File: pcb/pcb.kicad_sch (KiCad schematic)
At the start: 23 parts, among them J1 Conn_02x04_Odd_Even, J10 Conn_02x04_Odd_Even, J11 Conn_02x04_Odd_Even, J12 Conn_02x04_Odd_Even, J13 Conn_02x04_Odd_Even, J14 Conn_02x04_Odd_Even, J15 Conn_02x04_Odd_Even, J16 Conn_02x04_Odd_Even, J17 Conn_02x04_Odd_Even, J18 Conn_02x04_Odd_Even, J19 Conn_02x04_Odd_Even, J2 Conn_02x04_Odd_Even, J20 Conn_02x04_Odd_Even, J21 Conn_01x04_Pin, J3 Conn_02x04_Odd_Even, J4 Conn_02x04_Odd_Even, J5 Conn_02x04_Odd_Even, J6 Conn_02x04_Odd_Even, J7 Conn_02x04_Odd_Even, J8 Conn_02x04_Odd_Even, J9 Conn_02x04_Odd_Even

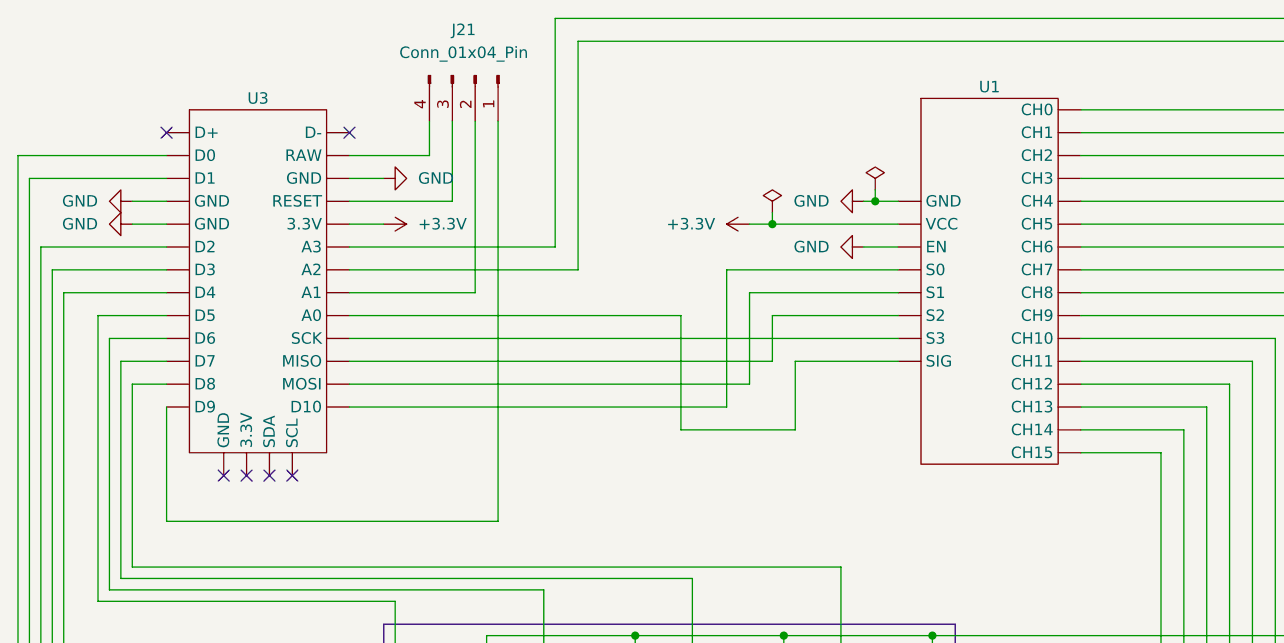
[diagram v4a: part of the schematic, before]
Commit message: header in documentation fixed, pcb schematic done
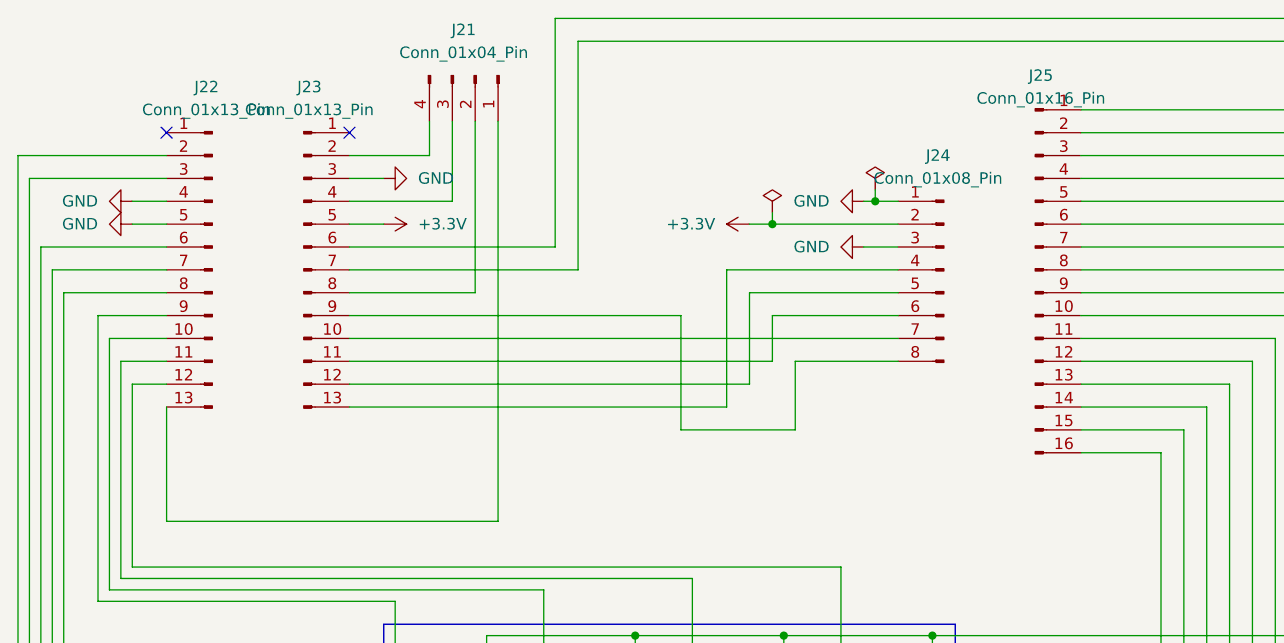
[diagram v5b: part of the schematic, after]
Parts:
- removed U1: ~, symbol analog_multiplexer:multiplexer
- removed U3: ~, symbol KB2040:KB2040
- added J22, J23: Conn_01x13_Pin, Connector_PinSocket_2.54mm:PinSocket_1x13_P2.54mm_Vertical, symbol Connector:Conn_01x13_Pin
- added J24: Conn_01x08_Pin, Connector_PinSocket_2.54mm:PinSocket_1x08_P2.54mm_Vertical, symbol Connector:Conn_01x08_Pin
- added J25: Conn_01x16_Pin, Connector_PinSocket_2.54mm:PinSocket_1x16_P2.54mm_Vertical, symbol Connector:Conn_01x16_Pin
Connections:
- net +3.3V: now also J23.5 (Pin_5), J24.2 (Pin_2)
- net GND: now also J22.4 (Pin_4), J22.5 (Pin_5), J23.3 (Pin_3), J24.1 (Pin_1), J24.3 (Pin_3)
- net at J14.3 (Pin_3): now also J25.10 (Pin_10)
- net at J10.4 (Pin_4), J14.4 (Pin_4), J18.4 (Pin_4)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: now also J22.10 (Pin_10)
- net at J13.6 (Pin_6), J14.6 (Pin_6), J15.6 (Pin_6)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: now also J22.7 (Pin_7)
- net at J1.7 (Pin_7), J10.7 (Pin_7), J11.7 (Pin_7)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: now also J23.6 (Pin_6)
- net at J1.8 (Pin_8), J10.8 (Pin_8), J11.8 (Pin_8)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: now also J23.7 (Pin_7)
- net at J21.1 (Pin_1): now also J22.13 (Pin_13)
- net at J21.2 (Pin_2): now also J23.8 (Pin_8)
- net at J21.3 (Pin_3): now also J23.4 (Pin_4)
- net at J21.4 (Pin_4): now also J23.2 (Pin_2)
- net at J6.3 (Pin_3): now also J25.2 (Pin_2)
- net at J5.6 (Pin_6), J6.6 (Pin_6), J7.6 (Pin_6)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: now also J22.3 (Pin_3)
- net at J10.3 (Pin_3): now also J25.6 (Pin_6)
- net at J10.6 (Pin_6), J11.6 (Pin_6), J12.6 (Pin_6)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: now also J22.6 (Pin_6)
- net at J5.3 (Pin_3): now also J25.1 (Pin_1)
- net at J1.4 (Pin_4), J13.4 (Pin_4), J17.4 (Pin_4)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: now also J22.9 (Pin_9)
- net at J12.3 (Pin_3): now also J25.8 (Pin_8)
- net at J12.4 (Pin_4), J16.4 (Pin_4), J20.4 (Pin_4)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: now also J22.12 (Pin_12)
- net at J20.3 (Pin_3): now also J25.16 (Pin_16)
- net at J17.6 (Pin_6), J18.6 (Pin_6), J19.6 (Pin_6)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: now also J22.8 (Pin_8)
- net at J1.6 (Pin_6), J2.6 (Pin_6), J3.6 (Pin_6)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: now also J22.2 (Pin_2)
- net at J13.3 (Pin_3): now also J25.9 (Pin_9)
- net at J18.3 (Pin_3): now also J25.14 (Pin_14)
- net at J7.3 (Pin_3): now also J25.3 (Pin_3)
- net at J11.4 (Pin_4), J15.4 (Pin_4), J19.4 (Pin_4)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: now also J22.11 (Pin_11)
- net at J11.3 (Pin_3): now also J25.7 (Pin_7)
- net at J17.3 (Pin_3): now also J25.13 (Pin_13)
- net at J16.3 (Pin_3): now also J25.12 (Pin_12)
- net at J15.3 (Pin_3): now also J25.11 (Pin_11)
- net at J9.3 (Pin_3): now also J25.5 (Pin_5)
- net at J8.3 (Pin_3): now also J25.4 (Pin_4)
- net at J19.3 (Pin_3): now also J25.15 (Pin_15)
- new net: J23.13 (Pin_13), J24.4 (Pin_4)
- new net: J23.12 (Pin_12), J24.5 (Pin_5)
- new net: J23.11 (Pin_11), J24.6 (Pin_6)
- new net: J23.10 (Pin_10), J24.7 (Pin_7)
- new net: J23.9 (Pin_9), J24.8 (Pin_8)
- no-connect marks 30 -> 26
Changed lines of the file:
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@@
   (no_connect (at 92.71 137.16))
   (no_connect (at 125.73 243.84))
-  (no_connect (at 54.61 66.04))
-  (no_connect (at 49.53 66.04))
   (no_connect (at 125.73 101.6))
   (no_connect (at 92.71 172.72))
@@
   (no_connect (at 123.19 243.84))
   (no_connect (at 92.71 208.28))
-  (no_connect (at 52.07 66.04))
   (no_connect (at 43.18 27.94))
   (no_connect (at 76.2 101.6))
   (no_connect (at 73.66 243.84))
   (no_connect (at 109.22 101.6))
-  (no_connect (at 57.15 66.04))
   (no_connect (at 76.2 208.28))
   (no_connect (at 92.71 101.6))
@@
     )
   )
+  (symbol (lib_id "Connector:Conn_01x13_Pin") (at 48.26 43.18 0) (mirror y) (unit 1)
+    (in_bom yes) (on_board yes) (dnp no)
+    (property "Reference" "J22" (at 47.625 22.86 0)
+      (effects (font (size 1.27 1.27)))
+    )
+    (property "Value" "Conn_01x13_Pin" (at 47.625 25.4 0)
+      (effects (font (size 1.27 1.27)))
+    )
+    (property "Footprint" "Connector_PinSocket_2.54mm:PinSocket_1x13_P2.54mm_Vertical" (at 48.26 43.18 0)
+      (effects (font (size 1.27 1.27)) hide)
+    )
+    (property "Datasheet" "~" (at 48.26 43.18 0)
+      (effects (font (size 1.27 1.27)) hide)
+    )
+    (pin "9")
+    (pin "13")
+    (pin "5")
+    (pin "8")
+    (pin "6")
+    (pin "7")
+    (pin "1")
+    (pin "12")
+    (pin "4")
+    (pin "10")
+    (pin "11")
+    (pin "2")
+    (pin "3")
+    (instances
+      (project "pcb"
+        (path "/7cd41366-658c-4c64-bfa9-b0a6b780fad4"
+          (reference "J22") (unit 1)
+        )
+      )
+    )
+  )
+  (symbol (lib_id "Connector:Conn_01x08_Pin") (at 129.54 43.18 0) (mirror y) (unit 1)
+    (in_bom yes) (on_board yes) (dnp no)
+    (property "Reference" "J24" (at 128.905 30.48 0)
+      (effects (font (size 1.27 1.27)))
+    )
+    (property "Value" "Conn_01x08_Pin" (at 128.905 33.02 0)
+      (effects (font (size 1.27 1.27)))
+    )
+    (property "Footprint" "Connector_PinSocket_2.54mm:PinSocket_1x08_P2.54mm_Vertical" (at 129.54 43.18 0)
+      (effects (font (size 1.27 1.27)) hide)
+    )
+    (property "Datasheet" "~" (at 129.54 43.18 0)
+      (effects (font (size 1.27 1.27)) hide)
+    )
+    (pin "1")
+    (pin "8")
+    (pin "6")
+    (pin "3")
+    (pin "7")
+    (pin "5")
+    (pin "4")
+    (pin "2")
+    (instances
+      (project "pcb"
+        (path "/7cd41366-658c-4c64-bfa9-b0a6b780fad4"
+          (reference "J24") (unit 1)
+        )
+      )
+    )
+  )
   (symbol (lib_id "power:GND") (at 104.14 243.84 0) (unit 1)
     (in_bom yes) (on_board yes) (dnp no) (fields_autoplaced)
@@
     )
   )
-  (symbol (lib_id "KB2040:KB2040") (at 53.34 41.91 0) (unit 1)
-    (in_bom yes) (on_board yes) (dnp no) (fields_autoplaced)
-    (property "Reference" "U3" (at 53.34 24.13 0)
-      (effects (font (size 1.27 1.27)))
-    )
-    (property "Value" "~" (at 57.15 36.83 0)
-      (effects (font (size 1.27 1.27)))
-    )
-    (property "Footprint" "" (at 57.15 36.83 0)
-      (effects (font (size 1.27 1.27)) hide)
-    )
-    (property "Datasheet" "" (at 57.15 36.83 0)
-      (effects (font (size 1.27 1.27)) hide)
-    )
-    (pin "")
-    (pin "")
-    (pin "")
-    (pin "")
-    (pin "")
-    (pin "")
-    (pin "")
-    (pin "")
-    (pin "")
-    (pin "")
-    (pin "")
-    (pin "")
-    (pin "")
-    (pin "")
-    (pin "")
-    (pin "")
-    (pin "")
-    (pin "")
-    (pin "")
-    (pin "")
-    (pin "")
-    (pin "")
-    (pin "")
-    (pin "")
-    (pin "")
-    (pin "")
-    (pin "")
-    (pin "")
-    (pin "")
-    (pin "")
-    (instances
-      (project "pcb"
-        (path "/7cd41366-658c-4c64-bfa9-b0a6b780fad4"
-          (reference "U3") (unit 1)
-        )
-      )
-    )
-  )
   (symbol (lib_id "Connector_Generic:Conn_02x04_Odd_Even") (at 123.19 132.08 90) (unit 1)
     (in_bom yes) (on_board yes) (dnp no)
@@
     )
   )
-  (symbol (lib_name "multiplexer_1") (lib_id "analog_multiplexer:multiplexer") (at 134.62 45.72 0) (unit 1)
-    (in_bom yes) (on_board yes) (dnp no) (fields_autoplaced)
-    (property "Reference" "U1" (at 134.62 22.86 0)
-      (effects (font (size 1.27 1.27)))
-    )
-    (property "Value" "~" (at 133.35 46.99 0)
-      (effects (font (size 1.27 1.27)))
-    )
-    (property "Footprint" "" (at 133.35 46.99 0)
-      (effects (font (size 1.27 1.27)) hide)
-    )
-    (property "Datasheet" "" (at 133.35 46.99 0)
-      (effects (font (size 1.27 1.27)) hide)
-    )
-    (pin "")
-    (pin "")
-    (pin "")
-    (pin "")
-    (pin "")
-    (pin "")
-    (pin "")
-    (pin "")
-    (pin "")
-    (pin "")
-    (pin "")
-    (pin "")
-    (pin "")
-    (pin "")
-    (pin "")
-    (pin "")
-    (pin "")
-    (pin "")
-    (pin "")
-    (pin "")
-    (pin "")
-    (pin "")
-    (pin "")
-    (pin "")
-    (instances
-      (project "pcb"
-        (path "/7cd41366-658c-4c64-bfa9-b0a6b780fad4"
-          (reference "U1") (unit 1)
-        )
-      )
-    )
-  )
   (symbol (lib_id "power:GND") (at 120.65 172.72 0) (unit 1)
     (in_bom yes) (on_board yes) (dnp no) (fields_autoplaced)
@@
     )
   )
+  (symbol (lib_id "Connector:Conn_01x13_Pin") (at 58.42 43.18 0) (unit 1)
+    (in_bom yes) (on_board yes) (dnp no)
+    (property "Reference" "J23" (at 59.055 22.86 0)
+      (effects (font (size 1.27 1.27)))
+    )
+    (property "Value" "Conn_01x13_Pin" (at 59.055 25.4 0)
+      (effects (font (size 1.27 1.27)))
+    )
+    (property "Footprint" "Connector_PinSocket_2.54mm:PinSocket_1x13_P2.54mm_Vertical" (at 58.42 43.18 0)
+      (effects (font (size 1.27 1.27)) hide)
+    )
+    (property "Datasheet" "~" (at 58.42 43.18 0)
+      (effects (font (size 1.27 1.27)) hide)
+    )
+    (pin "9")
+    (pin "13")
+    (pin "5")
+    (pin "8")
+    (pin "6")
+    (pin "7")
+    (pin "1")
+    (pin "12")
+    (pin "4")
+    (pin "10")
+    (pin "11")
+    (pin "2")
+    (pin "3")
+    (instances
+      (project "pcb"
+        (path "/7cd41366-658c-4c64-bfa9-b0a6b780fad4"
+          (reference "J23") (unit 1)
+        )
+      )
+    )
+  )
   (symbol (lib_id "power:+3.3V") (at 120.65 160.02 0) (unit 1)
     (in_bom yes) (on_board yes) (dnp no) (fields_autoplaced)
@@
         )
       )
+    )
+  )
+  (symbol (lib_id "Connector:Conn_01x16_Pin") (at 139.7 43.18 0) (unit 1)
+    (in_bom yes) (on_board yes) (dnp no) (fields_autoplaced)
+    (property "Reference" "J25" (at 140.335 21.59 0)
+      (effects (font (size 1.27 1.27)))
+    )
+    (property "Value" "Conn_01x16_Pin" (at 140.335 24.13 0)
+      (effects (font (size 1.27 1.27)))
+    )
+    (property "Footprint" "Connector_PinSocket_2.54mm:PinSocket_1x16_P2.54mm_Vertical" (at 139.7 43.18 0)
+      (effects (font (size 1.27 1.27)) hide)
+    )
+    (property "Datasheet" "~" (at 139.7 43.18 0)
+      (effects (font (size 1.27 1.27)) hide)
+    )
+    (pin "1")
+    (pin "5")
+    (pin "13")
+    (pin "4")
+    (pin "3")
+    (pin "7")
+    (pin "2")
+    (pin "6")
+    (pin "8")
+    (pin "15")
+    (pin "9")
+    (pin "11")
+    (pin "10")
+    (pin "12")
+    (pin "16")
+    (pin "14")
+    (instances
+      (project "pcb"
+        (path "/7cd41366-658c-4c64-bfa9-b0a6b780fad4"
+          (reference "J25") (unit 1)
+        )
+      )

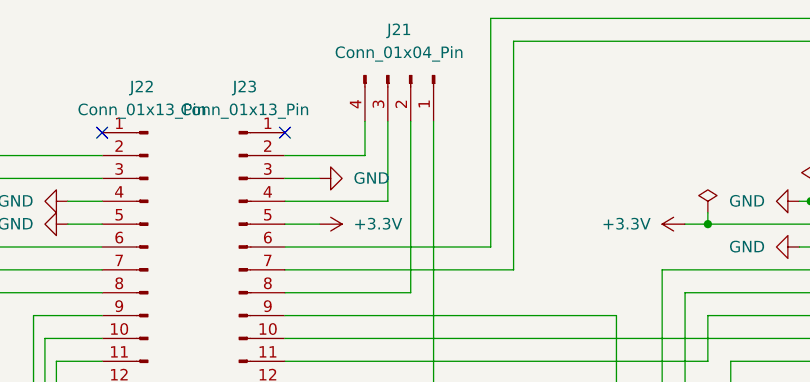
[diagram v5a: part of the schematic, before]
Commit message: pcb component placement
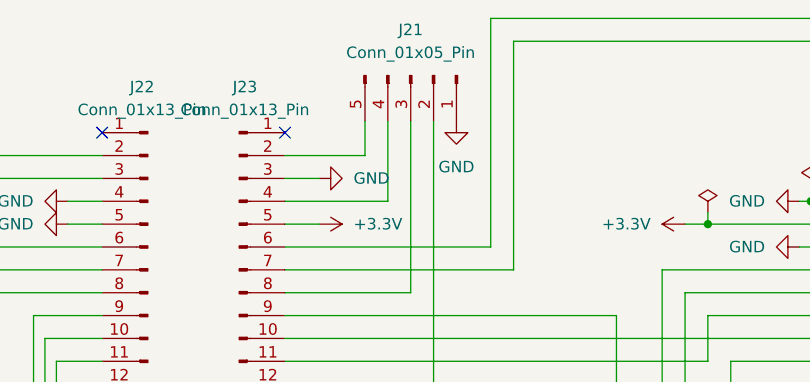
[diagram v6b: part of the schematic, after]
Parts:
- removed J21: Conn_01x04_Pin, Connector_PinHeader_2.54mm:PinHeader_1x04_P2.54mm_Vertical, symbol Connector:Conn_01x04_Pin
- added J21: Conn_01x05_Pin, Connector_PinHeader_2.54mm:PinHeader_1x05_P2.54mm_Vertical, symbol Connector:Conn_01x05_Pin
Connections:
- net GND: now also J21.1 (Pin_1)
- net at J22.13 (Pin_13): now also J21.2 (Pin_2)
- net at J23.8 (Pin_8): now also J21.3 (Pin_3)
- net at J23.4 (Pin_4): now also J21.4 (Pin_4)
- net at J23.2 (Pin_2): now also J21.5 (Pin_5)
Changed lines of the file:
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@@
     (fill (type color) (color 255 255 194 0.3))
+  )
+  (netclass_flag "" (length 2.54) (shape round) (at 67.31 30.48 0) (fields_autoplaced)
+    (effects (font (size 1.27 1.27)) (justify left bottom))
+    (property "Netclass" "RAW" (at 68.0085 27.94 0)
+      (effects (font (size 1.27 1.27) italic) (justify left))
+    )
+  )
+  (netclass_flag "" (length 2.54) (shape round) (at 64.77 38.1 0) (fields_autoplaced)
+    (effects (font (size 1.27 1.27)) (justify left bottom))
+    (property "Netclass" "3.3V" (at 65.4685 35.56 0)
+      (effects (font (size 1.27 1.27) italic) (justify left))
+    )
+  )
+  (netclass_flag "" (length 2.54) (shape round) (at 64.77 33.02 0) (fields_autoplaced)
+    (effects (font (size 1.27 1.27)) (justify left bottom))
+    (property "Netclass" "GND" (at 65.4685 30.48 0)
+      (effects (font (size 1.27 1.27) italic) (justify left))
+    )
   )
   (symbol (lib_id "power:+3.3V") (at 87.63 195.58 0) (unit 1)
@@
     )
   )
-  (symbol (lib_id "Connector:Conn_01x04_Pin") (at 77.47 21.59 270) (unit 1)
-    (in_bom yes) (on_board yes) (dnp no) (fields_autoplaced)
-    (property "Reference" "J21" (at 76.2 16.51 90)
-      (effects (font (size 1.27 1.27)))
-    )
-    (property "Value" "Conn_01x04_Pin" (at 76.2 19.05 90)
-      (effects (font (size 1.27 1.27)))
-    )
-    (property "Footprint" "Connector_PinHeader_2.54mm:PinHeader_1x04_P2.54mm_Vertical" (at 77.47 21.59 0)
-      (effects (font (size 1.27 1.27)) hide)
-    )
-    (property "Datasheet" "~" (at 77.47 21.59 0)
-      (effects (font (size 1.27 1.27)) hide)
-    )
-    (pin "1")
-    (pin "3")
-    (pin "4")
-    (pin "2")
-    (instances
-      (project "pcb"
-        (path "/7cd41366-658c-4c64-bfa9-b0a6b780fad4"
-          (reference "J21") (unit 1)
-        )
-      )
-    )
-  )
   (symbol (lib_id "power:GND") (at 87.63 101.6 0) (unit 1)
     (in_bom yes) (on_board yes) (dnp no) (fields_autoplaced)
@@
         (path "/7cd41366-658c-4c64-bfa9-b0a6b780fad4"
           (reference "J4") (unit 1)
+        )
+      )
+    )
+  )
+  (symbol (lib_id "Connector:Conn_01x05_Pin") (at 77.47 21.59 270) (unit 1)
+    (in_bom yes) (on_board yes) (dnp no) (fields_autoplaced)
+    (property "Reference" "J21" (at 77.47 16.51 90)
+      (effects (font (size 1.27 1.27)))
+    )
+    (property "Value" "Conn_01x05_Pin" (at 77.47 19.05 90)
+      (effects (font (size 1.27 1.27)))
+    )
+    (property "Footprint" "Connector_PinHeader_2.54mm:PinHeader_1x05_P2.54mm_Vertical" (at 77.47 21.59 0)
+      (effects (font (size 1.27 1.27)) hide)
+    )
+    (property "Datasheet" "~" (at 77.47 21.59 0)
+      (effects (font (size 1.27 1.27)) hide)
+    )
+    (pin "5")
+    (pin "3")
+    (pin "1")
+    (pin "2")
+    (pin "4")
+    (instances
+      (project "pcb"
+        (path "/7cd41366-658c-4c64-bfa9-b0a6b780fad4"
+          (reference "J21") (unit 1)
         )
       )
@@
         )
       )
+    )
+  )
+  (symbol (lib_id "power:GND") (at 82.55 26.67 0) (unit 1)
+    (in_bom yes) (on_board yes) (dnp no) (fields_autoplaced)
+    (property "Reference" "#PWR048" (at 82.55 33.02 0)
+      (effects (font (size 1.27 1.27)) hide)
+    )
+    (property "Value" "GND" (at 82.55 31.75 0)
+      (effects (font (size 1.27 1.27)))
+    )
+    (property "Footprint" "" (at 82.55 26.67 0)
+      (effects (font (size 1.27 1.27)) hide)
+    )
+    (property "Datasheet" "" (at 82.55 26.67 0)
+      (effects (font (size 1.27 1.27)) hide)
+    )
+    (pin "1")
+    (instances
+      (project "pcb"
+        (path "/7cd41366-658c-4c64-bfa9-b0a6b780fad4"
+          (reference "#PWR048") (unit 1)
+        )
+      )
